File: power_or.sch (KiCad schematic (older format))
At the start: 5 parts

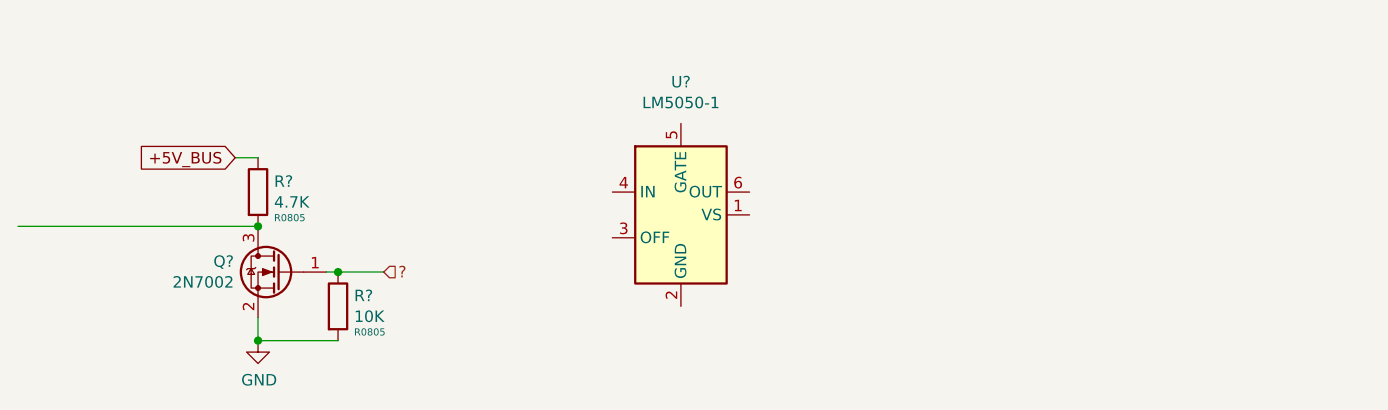
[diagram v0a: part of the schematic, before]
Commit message: add ina139
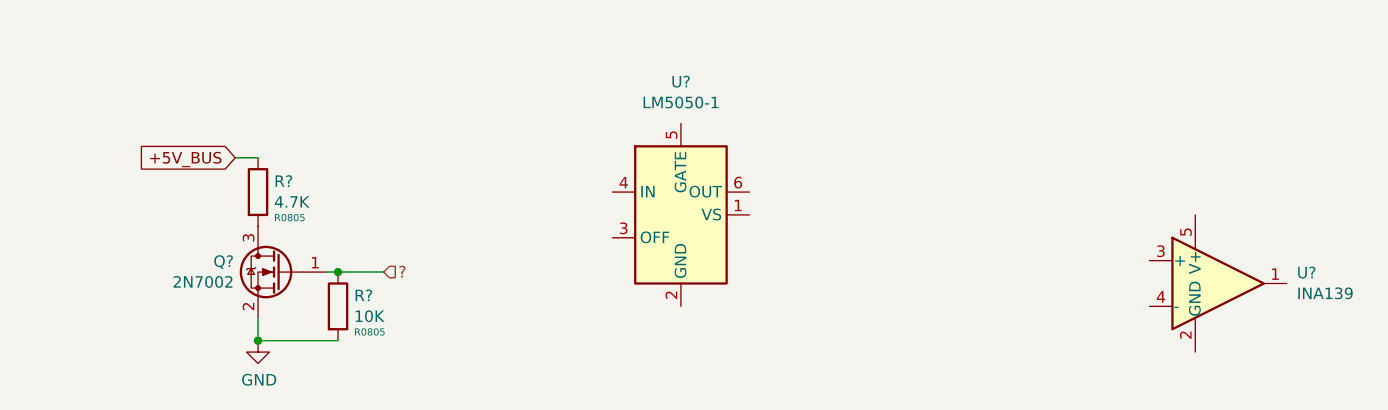
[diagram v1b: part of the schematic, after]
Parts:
- added U?: INA139, Package_TO_SOT_SMD:SOT-23-5, symbol Amplifier_Current:INA139
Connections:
- wire segments 6 -> 5
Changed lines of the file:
@@
 	2950 2950 3150 2950
 Connection ~ 2950 2950
-Wire Wire Line
-	1550 2750 2600 2750
 $Comp
 L Device:R R?
@@
 	1    0    0    -1
 $EndComp
-Connection ~ 2600 2750
 Wire Wire Line
 	2500 2450 2600 2450
@@
 	1    0    0    -1
 $EndComp
+$Comp
+L Amplifier_Current:INA139 U?
+U 1 1 5E3C04AF
+P 6800 3000
+F 0 "U?" H 7144 3046 50  0000 L CNN
+F 1 "INA139" H 7144 2955 50  0000 L CNN
+F 2 "Package_TO_SOT_SMD:SOT-23-5" H 6800 3000 50  0001 C CNN
+F 3 "http://www.ti.com/lit/gpn/ina139" H 6800 3005 50  0001 C CNN
+	1    6800 3000
+	1    0    0    -1
+$EndComp

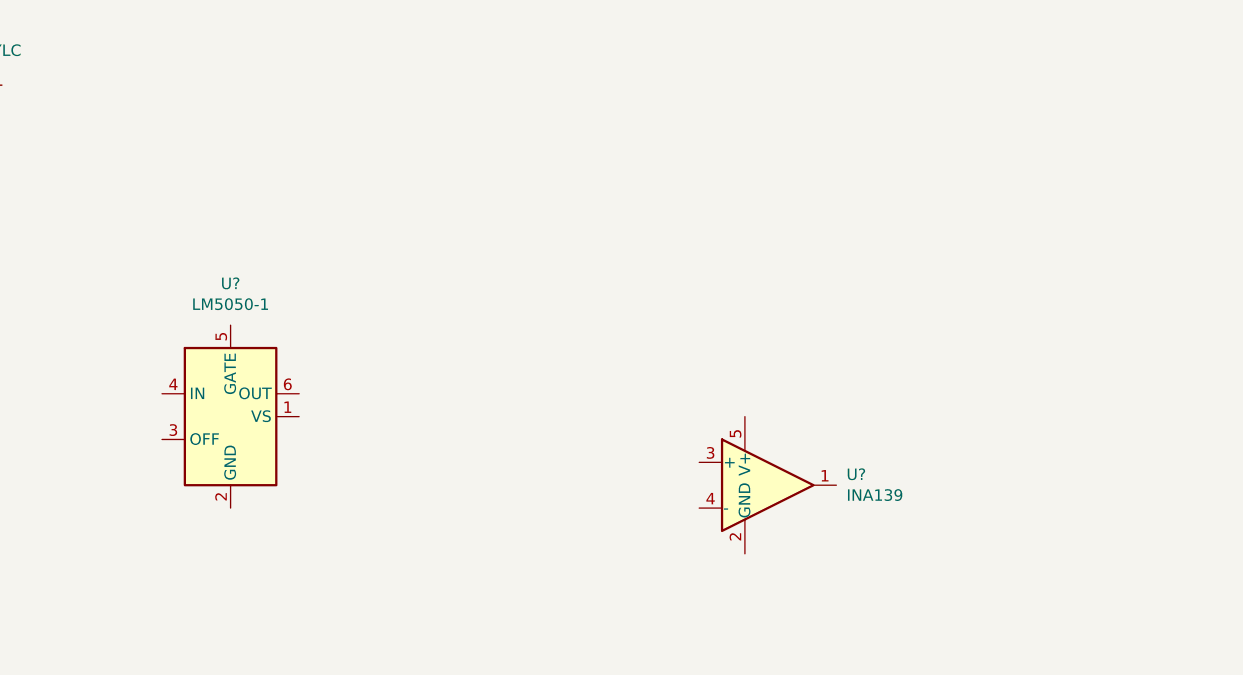
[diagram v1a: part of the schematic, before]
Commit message: add 0.5mR R2725
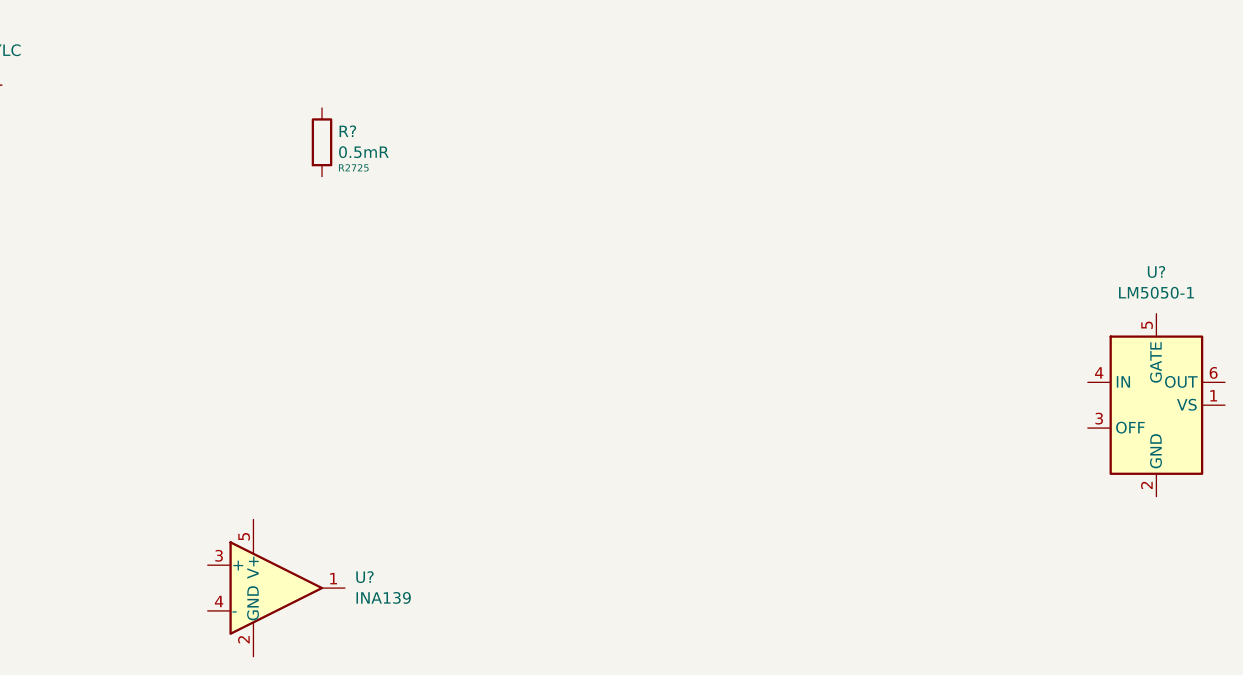
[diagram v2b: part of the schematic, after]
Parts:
- added R?: 0.5mR, Resistor_SMD:R_2725_6865Metric, symbol Device:R
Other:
- moved on the sheet: U?
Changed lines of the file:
@@
 AR Path="/5E300FCE/5E3BCD4C" Ref="R?"  Part="1"
 AR Path="/5E350920/5E3BCD4C" Ref="R?"  Part="1"
+AR Path="/5E3BA3E9/5E3BCD4C" Ref="R?"  Part="1"
 F 0 "R?" H 3020 3146 50  0000 L CNN
 F 1 "10K" H 3020 3055 50  0000 L CNN
@@
 AR Path="/5E300FCE/5E3BCD5A" Ref="R?"  Part="1"
 AR Path="/5E350920/5E3BCD5A" Ref="R?"  Part="1"
+AR Path="/5E3BA3E9/5E3BCD5A" Ref="R?"  Part="1"
 F 0 "R?" H 2670 2646 50  0000 L CNN
 F 1 "4.7K" H 2670 2555 50  0000 L CNN
@@
 L Power_Management:LM5050-1 U?
 U 1 1 5E3BDD42
-P 4450 2700
-F 0 "U?" H 4450 3281 50  0000 C CNN
-F 1 "LM5050-1" H 4450 3190 50  0000 C CNN
-F 2 "Package_TO_SOT_SMD:TSOT-23-6" H 5100 2350 50  0001 C CNN
-F 3 "http://www.ti.com/lit/ds/symlink/lm5050-1-q1.pdf" H 5550 2650 50  0001 C CNN
-	1    4450 2700
+P 8500 2650
+F 0 "U?" H 8500 3231 50  0000 C CNN
+F 1 "LM5050-1" H 8500 3140 50  0000 C CNN
+F 2 "Package_TO_SOT_SMD:TSOT-23-6" H 9150 2300 50  0001 C CNN
+F 3 "http://www.ti.com/lit/ds/symlink/lm5050-1-q1.pdf" H 9600 2600 50  0001 C CNN
+	1    8500 2650
 	1    0    0    -1
 $EndComp
@@
 L Amplifier_Current:INA139 U?
 U 1 1 5E3C04AF
-P 6800 3000
-F 0 "U?" H 7144 3046 50  0000 L CNN
-F 1 "INA139" H 7144 2955 50  0000 L CNN
-F 2 "Package_TO_SOT_SMD:SOT-23-5" H 6800 3000 50  0001 C CNN
-F 3 "http://www.ti.com/lit/gpn/ina139" H 6800 3005 50  0001 C CNN
-	1    6800 3000
+P 4650 3450
+F 0 "U?" H 4994 3496 50  0000 L CNN
+F 1 "INA139" H 4994 3405 50  0000 L CNN
+F 2 "Package_TO_SOT_SMD:SOT-23-5" H 4650 3450 50  0001 C CNN
+F 3 "http://www.ti.com/lit/gpn/ina139" H 4650 3455 50  0001 C CNN
+	1    4650 3450
 	1    0    0    -1
 $EndComp
+$Comp
+L Device:R R?
+U 1 1 5E36544B
+P 4850 1500
+AR Path="/5E300FCE/5E36544B" Ref="R?"  Part="1"
+AR Path="/5E350920/5E36544B" Ref="R?"  Part="1"
+AR Path="/5E3BA3E9/5E36544B" Ref="R?"  Part="1"
+F 0 "R?" H 4920 1546 50  0000 L CNN
+F 1 "0.5mR" H 4920 1455 50  0000 L CNN
+F 2 "Resistor_SMD:R_2725_6865Metric" V 4780 1500 50  0001 C CNN
+F 3 "~" H 4850 1500 50  0001 C CNN
+F 4 "R2725" H 4920 1387 31  0000 L CNN "size"
+	1    4850 1500
+	1    0    0    -1
+$EndComp

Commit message: pause on power or
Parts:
- added C?: 100pF, Capacitor_SMD:C_0805_2012Metric, symbol Device:C
- added C? (x2): 10uF, Capacitor_SMD:C_1206_3216Metric, symbol Device:C
- added C?: 25V 10uF, Capacitor_SMD:C_1206_3216Metric, symbol Device:C
- added C?: 50V 100pF, Capacitor_SMD:C_0805_2012Metric, symbol Device:C
- added D?: 1.5KExxA, Diode_THT:D_DO-201AE_P15.24mm_Horizontal, symbol Diode:1.5KExxA
- added U?: LM1117-3.3, Package_TO_SOT_SMD:SOT-223-3_TabPin2, symbol Regulator_Linear:LM1117-3.3
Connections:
- net labels added: +12V_BUS, +12V_IN, +3V3, +5V_IN
- wire segments 5 -> 28
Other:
- moved on the sheet: R?
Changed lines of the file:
@@
 L Device:R R?
 U 1 1 5E36544B
-P 4850 1500
+P 3950 3450
 AR Path="/5E300FCE/5E36544B" Ref="R?"  Part="1"
 AR Path="/5E350920/5E36544B" Ref="R?"  Part="1"
 AR Path="/5E3BA3E9/5E36544B" Ref="R?"  Part="1"
-F 0 "R?" H 4920 1546 50  0000 L CNN
-F 1 "0.5mR" H 4920 1455 50  0000 L CNN
-F 2 "Resistor_SMD:R_2725_6865Metric" V 4780 1500 50  0001 C CNN
-F 3 "~" H 4850 1500 50  0001 C CNN
-F 4 "R2725" H 4920 1387 31  0000 L CNN "size"
-	1    4850 1500
-	1    0    0    -1
-$EndComp
+F 0 "R?" H 4020 3496 50  0000 L CNN
+F 1 "0.5mR" H 4020 3405 50  0000 L CNN
+F 2 "Resistor_SMD:R_2725_6865Metric" V 3880 3450 50  0001 C CNN
+F 3 "~" H 3950 3450 50  0001 C CNN
+F 4 "R2725" H 4020 3337 31  0000 L CNN "size"
+	1    3950 3450
+	1    0    0    -1
+$EndComp
+$Comp
+L Regulator_Linear:LM1117-3.3 U?
+U 1 1 5E3A6247
+P 4750 6750
+AR Path="/5E3022E2/5E3A6247" Ref="U?"  Part="1"
+AR Path="/5E3BA3E9/5E3A6247" Ref="U?"  Part="1"
+F 0 "U?" H 4750 6992 50  0000 C CNN
+F 1 "LM1117-3.3" H 4750 6901 50  0000 C CNN
+F 2 "Package_TO_SOT_SMD:SOT-223-3_TabPin2" H 4750 6750 50  0001 C CNN
+F 3 "http://www.ti.com/lit/ds/symlink/lm1117.pdf" H 4750 6750 50  0001 C CNN
+	1    4750 6750
+	1    0    0    -1
+$EndComp
+$Comp
+L power:+3V3 #PWR?
+U 1 1 5E3A624D
+P 6300 6750
+AR Path="/5E300FCE/5E3A624D" Ref="#PWR?"  Part="1"
+AR Path="/5E3022E2/5E3A624D" Ref="#PWR?"  Part="1"
+AR Path="/5E3BA3E9/5E3A624D" Ref="#PWR?"  Part="1"
+F 0 "#PWR?" H 6300 6600 50  0001 C CNN
+F 1 "+3V3" H 6315 6923 50  0000 C CNN
+F 2 "" H 6300 6750 50  0001 C CNN
+F 3 "" H 6300 6750 50  0001 C CNN
+	1    6300 6750
+	1    0    0    -1
+$EndComp
+$Comp
+L power:GND #PWR?
+U 1 1 5E3A6253
+P 4750 7300
+AR Path="/5E300FCE/5E3A6253" Ref="#PWR?"  Part="1"
+AR Path="/5E3022E2/5E3A6253" Ref="#PWR?"  Part="1"
+AR Path="/5E3BA3E9/5E3A6253" Ref="#PWR?"  Part="1"
+F 0 "#PWR?" H 4750 7050 50  0001 C CNN
+F 1 "GND" H 4755 7127 50  0000 C CNN
+F 2 "" H 4750 7300 50  0001 C CNN
+F 3 "" H 4750 7300 50  0001 C CNN
+	1    4750 7300
+	1    0    0    -1
+$EndComp
+Wire Wire Line
+	6300 7250 6300 7150
+Wire Wire Line
+	6300 6750 6300 6850
+Wire Wire Line
+	5750 7250 5200 7250
+Connection ~ 5750 6750
+Wire Wire Line
+	5750 6750 5200 6750
+Wire Wire Line
+	5750 7150 5750 7250
+Wire Wire Line
+	5200 7250 5200 7150
+Wire Wire Line
+	5200 6750 5200 6850
+Wire Wire Line
+	5750 6850 5750 6750
+Wire Wire Line
+	5750 7250 6300 7250
+Connection ~ 5750 7250
+Wire Wire Line
+	5750 6750 6300 6750
+Connection ~ 6300 6750
+$Comp
+L Device:C C?
+U 1 1 5E3A6267
+P 5200 7000
+AR Path="/5E350920/5E3A6267" Ref="C?"  Part="1"
+AR Path="/5E31859C/5E3A6267" Ref="C?"  Part="1"
+AR Path="/5E3022E2/5E3A6267" Ref="C?"  Part="1"
+AR Path="/5E3BA3E9/5E3A6267" Ref="C?"  Part="1"
+F 0 "C?" H 5315 7091 50  0000 L CNN
+F 1 "100pF" H 5315 7000 50  0000 L CNN
+F 2 "Capacitor_SMD:C_0805_2012Metric" H 5238 6850 50  0001 C CNN
+F 3 "~" H 5200 7000 50  0001 C CNN
+F 4 "C0805" H 5315 6909 50  0000 L CNN "size"
+	1    5200 7000
+	1    0    0    -1
+$EndComp
+$Comp
+L Device:C C?
+U 1 1 5E3A626E
+P 5750 7000
+AR Path="/5E350920/5E3A626E" Ref="C?"  Part="1"
+AR Path="/5E31859C/5E3A626E" Ref="C?"  Part="1"
+AR Path="/5E3022E2/5E3A626E" Ref="C?"  Part="1"
+AR Path="/5E3BA3E9/5E3A626E" Ref="C?"  Part="1"
+F 0 "C?" H 5865 7091 50  0000 L CNN
+F 1 "10uF" H 5865 7000 50  0000 L CNN
+F 2 "Capacitor_SMD:C_1206_3216Metric" H 5788 6850 50  0001 C CNN
+F 3 "~" H 5750 7000 50  0001 C CNN
+F 4 "C1206" H 5865 6909 50  0000 L CNN "size"
+	1    5750 7000
+	1    0    0    -1
+$EndComp
+$Comp
+L Device:C C?
+U 1 1 5E3A6275
+P 6300 7000
+AR Path="/5E350920/5E3A6275" Ref="C?"  Part="1"
+AR Path="/5E31859C/5E3A6275" Ref="C?"  Part="1"
+AR Path="/5E3022E2/5E3A6275" Ref="C?"  Part="1"
+AR Path="/5E3BA3E9/5E3A6275" Ref="C?"  Part="1"
+F 0 "C?" H 6415 7091 50  0000 L CNN
+F 1 "10uF" H 6415 7000 50  0000 L CNN
+F 2 "Capacitor_SMD:C_1206_3216Metric" H 6338 6850 50  0001 C CNN
+F 3 "~" H 6300 7000 50  0001 C CNN
+F 4 "C1206" H 6415 6909 50  0000 L CNN "size"
+	1    6300 7000
+	1    0    0    -1
+$EndComp
+Wire Wire Line
+	4750 7050 4750 7250
+Wire Wire Line
+	5200 7250 4750 7250
+Connection ~ 5200 7250
+Connection ~ 4750 7250
+Wire Wire Line
+	4750 7250 4750 7300
+Wire Wire Line
+	5050 6750 5200 6750
+Connection ~ 5200 6750
+Wire Wire Line
+	3950 7250 3950 7150
+Wire Wire Line
+	3950 6750 3950 6850
+Connection ~ 3250 6750
+Wire Wire Line
+	3250 6750 3000 6750
+Wire Wire Line
+	3250 6850 3250 6750
+Wire Wire Line
+	3250 6750 3950 6750
+$Comp
+L Device:C C?
+U 1 1 5E3A6289
+P 3950 7000
+AR Path="/5E350920/5E3A6289" Ref="C?"  Part="1"
+AR Path="/5E31859C/5E3A6289" Ref="C?"  Part="1"
+AR Path="/5E3022E2/5E3A6289" Ref="C?"  Part="1"
+AR Path="/5E3BA3E9/5E3A6289" Ref="C?"  Part="1"
+F 0 "C?" H 4065 7091 50  0000 L CNN
+F 1 "25V 10uF" H 4065 7000 50  0000 L CNN
+F 2 "Capacitor_SMD:C_1206_3216Metric" H 3988 6850 50  0001 C CNN
+F 3 "~" H 3950 7000 50  0001 C CNN
+F 4 "C1206" H 4065 6909 50  0000 L CNN "size"
+	1    3950 7000
+	1    0    0    -1
+$EndComp
+Wire Wire Line
+	3250 7250 3950 7250
+Wire Wire Line
+	3250 7150 3250 7250
+Wire Wire Line
+	3950 7250 4750 7250
+Connection ~ 3950 7250
+Wire Wire Line
+	4450 6750 3950 6750
+Connection ~ 3950 6750
+$Comp
+L Device:C C?
+U 1 1 5E3A6296
+P 3250 7000
+AR Path="/5E350920/5E3A6296" Ref="C?"  Part="1"
+AR Path="/5E31859C/5E3A6296" Ref="C?"  Part="1"
+AR Path="/5E3022E2/5E3A6296" Ref="C?"  Part="1"
+AR Path="/5E3BA3E9/5E3A6296" Ref="C?"  Part="1"
+F 0 "C?" H 3365 7091 50  0000 L CNN
+F 1 "50V 100pF" H 3365 7000 50  0000 L CNN
+F 2 "Capacitor_SMD:C_0805_2012Metric" H 3288 6850 50  0001 C CNN
+F 3 "~" H 3250 7000 50  0001 C CNN
+F 4 "C0805" H 3365 6909 50  0000 L CNN "size"
+	1    3250 7000
+	1    0    0    -1
+$EndComp
+Text GLabel 750  7300 1    50   Input ~ 0
++12V_IN
+Text GLabel 1400 7300 1    50   Input ~ 0
++12V_BUS
+Text GLabel 4950 4500 1    50   Input ~ 0
++5V_IN
+Text GLabel 5200 4500 1    50   Input ~ 0
++5V_BUS
+$Comp
+L Diode:1.5KExxA D?
+U 1 1 5E3CDAEA
+P 7250 2200
+F 0 "D?" H 7250 2417 50  0000 C CNN
+F 1 "1.5KExxA" H 7250 2326 50  0000 C CNN
+F 2 "Diode_THT:D_DO-201AE_P15.24mm_Horizontal" H 7250 2000 50  0001 C CNN
+F 3 "https://www.vishay.com/docs/88301/15ke.pdf" H 7200 2200 50  0001 C CNN
+	1    7250 2200
+	1    0    0    -1
+$EndComp

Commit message: pause at power or
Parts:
- removed D?: 1.5KExxA, Diode_THT:D_DO-201AE_P15.24mm_Horizontal, symbol Diode:1.5KExxA
- removed R?: 0.5mR, Resistor_SMD:R_2725_6865Metric, symbol Device:R
- added C?: 2.2uF, Capacitor_SMD:C_1206_3216Metric, symbol Device:C
- added C? (x3): 100pF, Capacitor_SMD:C_0805_2012Metric, symbol Device:C
- added C? (x3): 1uF, Capacitor_SMD:C_0805_2012Metric, symbol Device:C
- added D? (x2): SMBJxxxAQ, Diode_SMD:D_SMB, symbol Diode:SMBJxxxAQ
- added Q?: PSMN1R8-40YLC, Package_TO_SOT_SMD:LFPAK56, symbol Transistor_FET:PSMN1R8-40YLC
- added R?: 100R, Resistor_SMD:R_0805_2012Metric, symbol Device:R
- added R?: 10K, Resistor_SMD:R_0805_2012Metric, symbol Device:R
- added R?: 0.5mR, Resistor_SMD:R_2725_6865Metric, symbol Device:R
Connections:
- wire segments 28 -> 93
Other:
- moved on the sheet: U?
